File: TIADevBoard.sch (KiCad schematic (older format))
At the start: 41 parts, among them J1 Screw_Terminal_01x02, J2 Conn_Coaxial, J3 Conn_Coaxial, J4 Conn_02x03_Counter_Clockwise, J5 Conn_Coaxial, U1 MC33063AD, U2 OPA2387, U3 ADP3330-3, U4 ADP7183

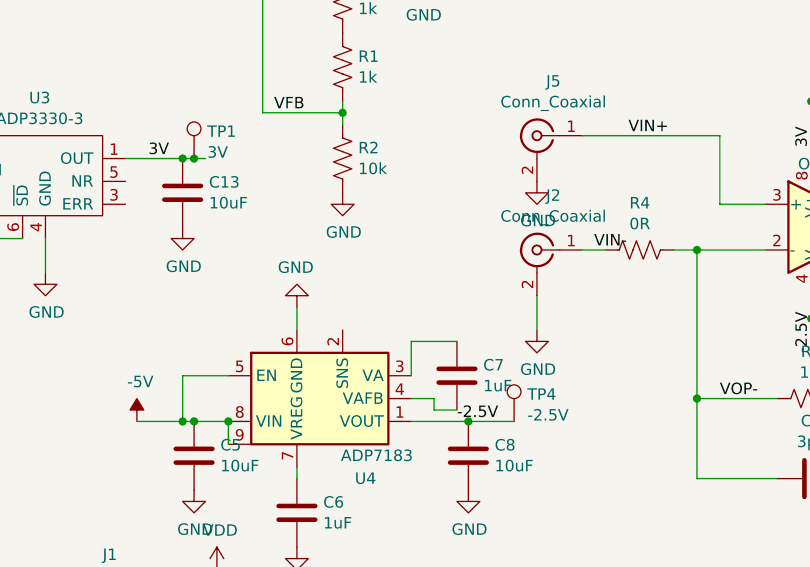
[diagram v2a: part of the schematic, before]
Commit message: fixed some errors in version 3 of PCB, updated the README to that effect.
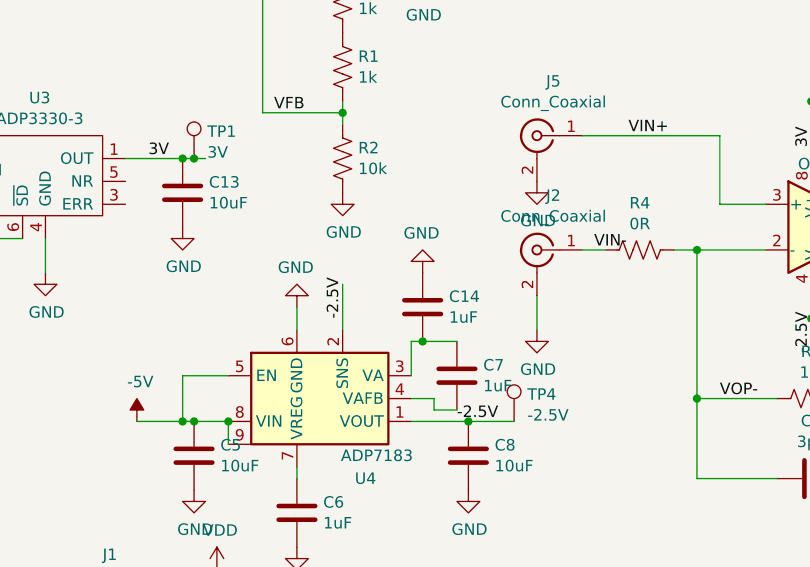
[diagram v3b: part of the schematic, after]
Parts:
- added C14: 1uF, Capacitor_SMD:C_0805_2012Metric_Pad1.15x1.40mm_HandSolder, symbol Device:C
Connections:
- wire segments 102 -> 104
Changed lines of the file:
@@
-$EndComp
-$Comp
-L Device:R_US R2
-U 1 1 6001BAE8
-P 2900 3600
-F 0 "R2" H 2968 3646 50  0000 L CNN
-F 1 "10k" H 2968 3555 50  0000 L CNN
-F 2 "Resistor_SMD:R_0805_2012Metric_Pad1.15x1.40mm_HandSolder" V 2940 3590 50  0001 C CNN
-F 3 "~" H 2900 3600 50  0001 C CNN
-	1    2900 3600
-	1    0    0    -1
 $EndComp
 $Comp
@@
 	3200 4550 3200 4400
 Wire Wire Line
-	3200 4400 3400 4400
+	3200 4400 3250 4400
 Wire Wire Line
 	3200 4650 3300 4650
@@
 Text Label 4150 3500 0    50   ~ 0
 VIN+
+$Comp
+L Device:R_US R2
+U 1 1 6001BAE8
+P 2900 3600
+F 0 "R2" H 2968 3646 50  0000 L CNN
+F 1 "10k" H 2968 3555 50  0000 L CNN
+F 2 "Resistor_SMD:R_0805_2012Metric_Pad1.15x1.40mm_HandSolder" V 2940 3590 50  0001 C CNN
+F 3 "~" H 2900 3600 50  0001 C CNN
+	1    2900 3600
+	1    0    0    -1
+$EndComp
+Wire Wire Line
+	2900 4350 2900 4150
+Text Label 2900 4300 1    50   ~ 0
+-2.5V
+$Comp
+L Device:C C14
+U 1 1 602255CD
+P 3250 4250
+F 0 "C14" H 3365 4296 50  0000 L CNN
+F 1 "1uF" H 3365 4205 50  0000 L CNN
+F 2 "Capacitor_SMD:C_0805_2012Metric_Pad1.15x1.40mm_HandSolder" H 3288 4100 50  0001 C CNN
+F 3 "~" H 3250 4250 50  0001 C CNN
+	1    3250 4250
+	1    0    0    -1
+$EndComp
+Connection ~ 3250 4400
+Wire Wire Line
+	3250 4400 3400 4400
+$Comp
+L power:GND #PWR014
+U 1 1 602262B8
+P 3250 4100
+F 0 "#PWR014" H 3250 3850 50  0001 C CNN
+F 1 "GND" H 3255 3927 50  0000 C CNN
+F 2 "" H 3250 4100 50  0001 C CNN
+F 3 "" H 3250 4100 50  0001 C CNN
+	1    3250 4100
+	-1   0    0    1
+$EndComp
 $EndSCHEMATC

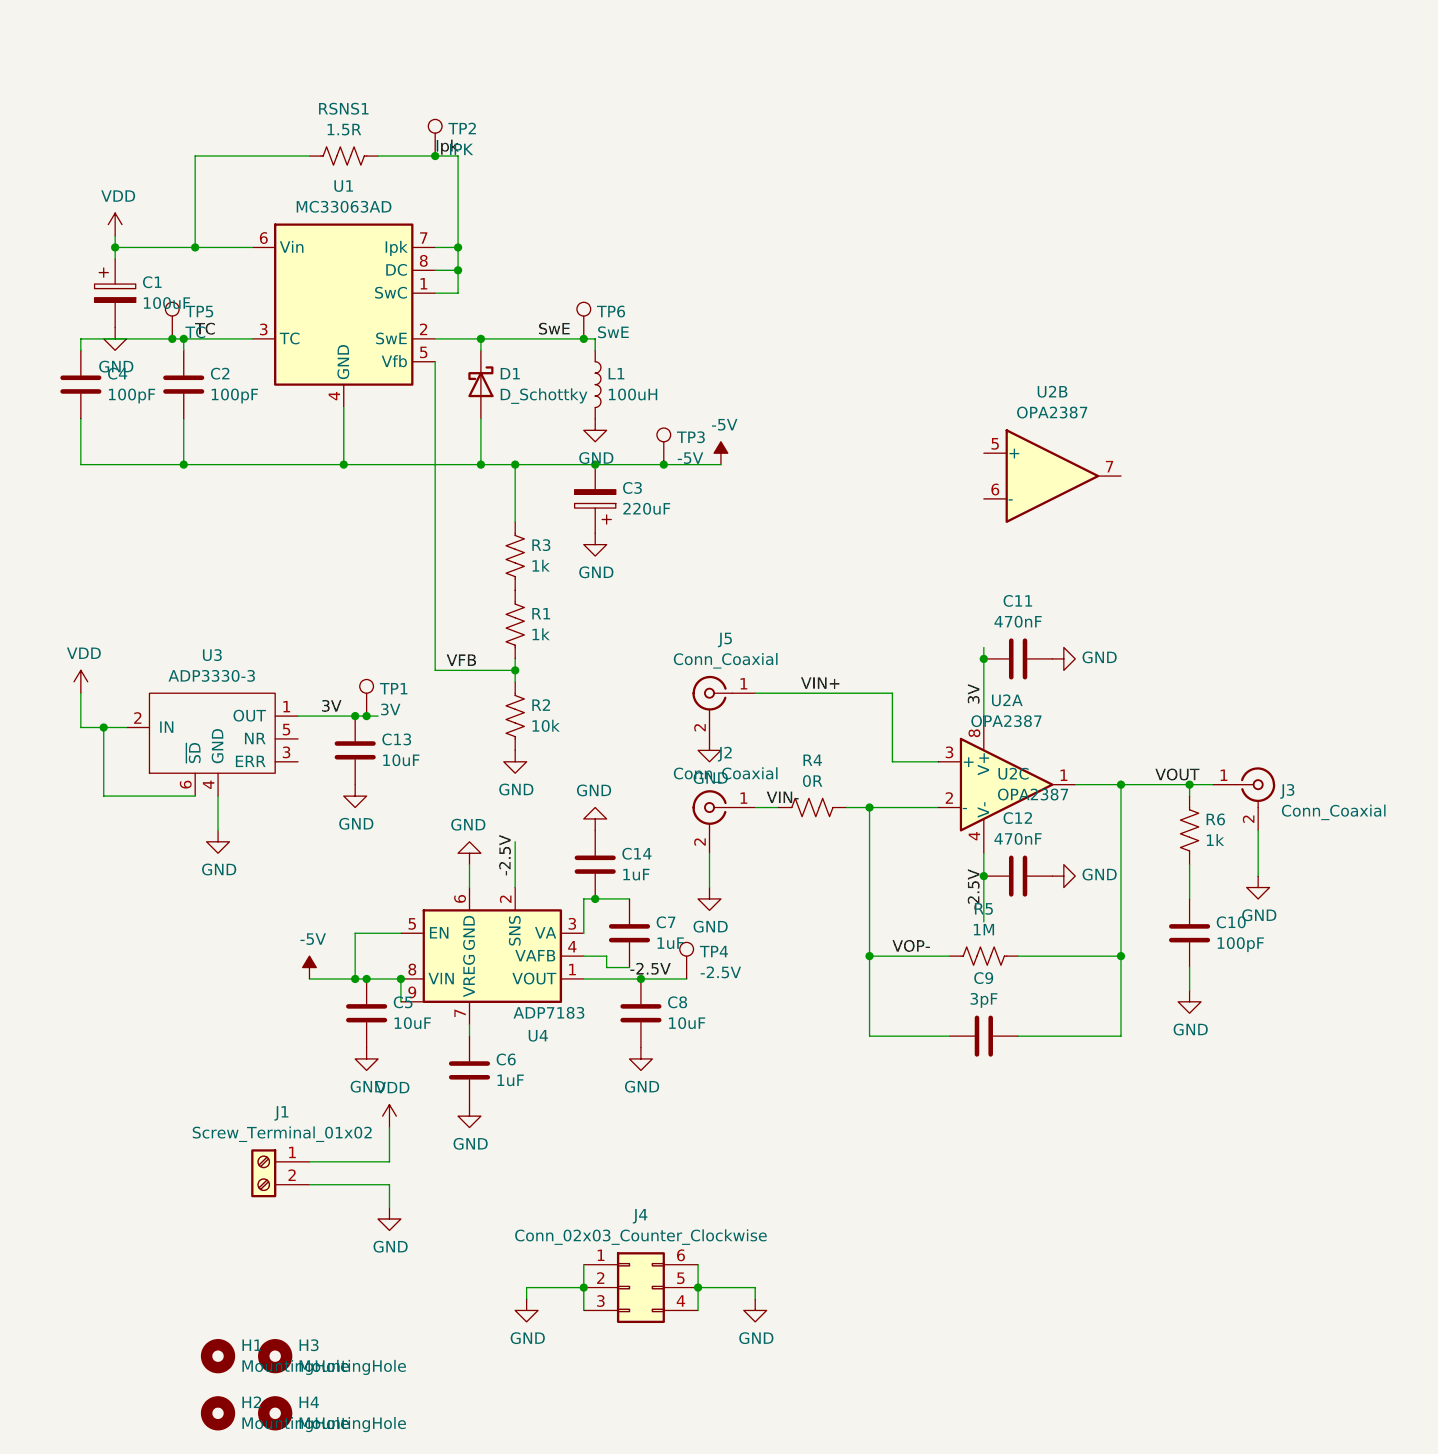
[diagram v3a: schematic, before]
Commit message: partial redesign of TIA v4, removed boost/buck converter, -2.5V linear regulator, added in second opamp in unity gain configuration with bias voltage. Layout not complete.
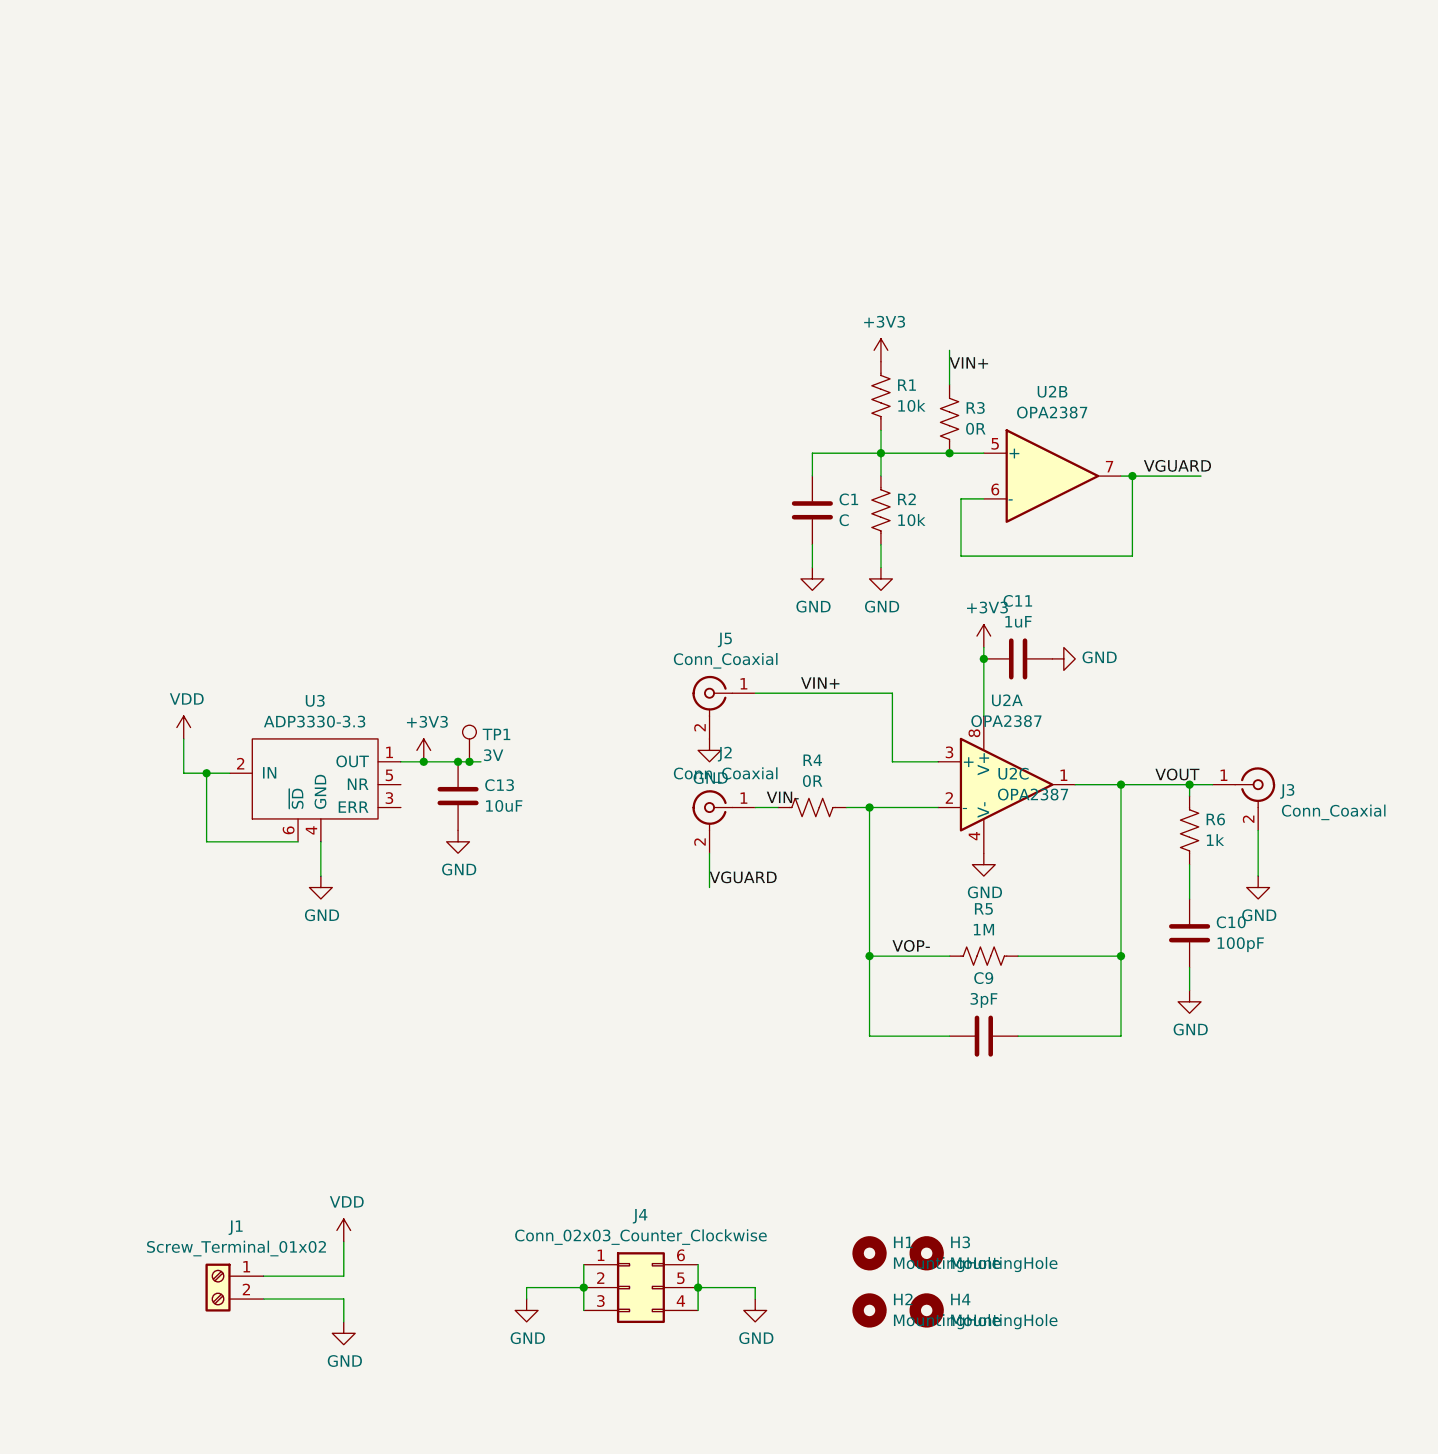
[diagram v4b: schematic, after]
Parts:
- removed C1: 100uF, Capacitor_THT:CP_Radial_D8.0mm_P5.00mm, symbol Device:CP
- removed C12: 470nF, Capacitor_SMD:C_0805_2012Metric_Pad1.15x1.40mm_HandSolder, symbol Device:C
- removed C14, C6, C7: 1uF, Capacitor_SMD:C_0805_2012Metric_Pad1.15x1.40mm_HandSolder, symbol Device:C
- removed C2, C4: 100pF, Capacitor_SMD:C_0805_2012Metric_Pad1.15x1.40mm_HandSolder, symbol Device:C
- removed C3: 220uF, Capacitor_THT:CP_Radial_D8.0mm_P5.00mm, symbol Device:CP
- removed C5, C8: 10uF, Capacitor_SMD:C_0805_2012Metric_Pad1.15x1.40mm_HandSolder, symbol Device:C
- removed D1: D_Schottky, Diode_SMD:D_SMA_Handsoldering, symbol Device:D_Schottky
- removed L1: 100uH, Inductor_SMD:L_1210_3225Metric_Pad1.42x2.65mm_HandSolder, symbol Device:L
- removed RSNS1: 1.5R, Resistor_SMD:R_0805_2012Metric_Pad1.15x1.40mm_HandSolder, symbol Device:R_US
- removed TP2: IPK, my_library_foot:TestPoint_Keystone_5000-5004_Miniature, symbol Connector:TestPoint
- removed TP3: -5V, my_library_foot:TestPoint_Keystone_5000-5004_Miniature, symbol Connector:TestPoint
- removed TP4: -2.5V, my_library_foot:TestPoint_Keystone_5000-5004_Miniature, symbol Connector:TestPoint
- removed TP5: TC, my_library_foot:TestPoint_Keystone_5000-5004_Miniature, symbol Connector:TestPoint
- removed TP6: SwE, my_library_foot:TestPoint_Keystone_5000-5004_Miniature, symbol Connector:TestPoint
- removed U1: MC33063AD, Package_SO:SOIC-8_3.9x4.9mm_P1.27mm, symbol Regulator_Switching:MC33063AD
- removed U4: ADP7183, Package_CSP:LFCSP-8-1EP_2x2mm_P0.5mm_EP1.5x1.0mm, symbol my_library:ADP7183
- added C1: C, Capacitor_SMD:C_0805_2012Metric_Pad1.15x1.40mm_HandSolder, symbol Device:C
- C11: value 470nF -> 1uF
- R1: value 1k -> 10k
- R3: value 1k -> 0R
- U3: value ADP3330-3 -> ADP3330-3.3
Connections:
- net labels added: +3V3, VGUARD
- net labels removed: -2.5V, -5V, 3V, Ipk, SwE, TC, VFB
- wire segments 104 -> 61
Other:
- moved on the sheet: C13, H1, H2, H3, H4, J1, TP1, U3

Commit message: added gerbers for version 5
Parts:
- removed C10: 100pF, Capacitor_SMD:C_0805_2012Metric_Pad1.15x1.40mm_HandSolder, symbol Device:C
- removed J1: Screw_Terminal_01x02, TerminalBlock:TerminalBlock_Altech_AK300-2_P5.00mm, symbol Connector:Screw_Terminal_01x02
- removed J5: Conn_Coaxial, my_library_foot:CON-SMA-EDGE-S, symbol Connector:Conn_Coaxial
- removed R3: 0R, Resistor_SMD:R_0805_2012Metric_Pad1.15x1.40mm_HandSolder, symbol Device:R_US
- removed R6: 1k, Resistor_SMD:R_0805_2012Metric_Pad1.15x1.40mm_HandSolder, symbol Device:R_US
- removed U2: OPA2387, Package_SO:VSSOP-8_3.0x3.0mm_P0.65mm, symbol my_library:OPA2387
- added C3: 1uF, Capacitor_SMD:C_0805_2012Metric_Pad1.15x1.40mm_HandSolder, symbol Device:C
- added C4: 10nF, Capacitor_SMD:C_0805_2012Metric_Pad1.15x1.40mm_HandSolder, symbol Device:C
- added C5, C6, C7: 10uF, Capacitor_SMD:C_0805_2012Metric_Pad1.15x1.40mm_HandSolder, symbol Device:C
- added C8: 100nF, Capacitor_SMD:C_0805_2012Metric_Pad1.15x1.40mm_HandSolder, symbol Device:C
- added CFF1: 100pF, Capacitor_SMD:C_0805_2012Metric_Pad1.15x1.40mm_HandSolder, symbol Device:C
- added D1: D, Diode_SMD:D_SOD-323_HandSoldering, symbol Device:D
- added J1: Jack-DC, Connector_BarrelJack:BarrelJack_Horizontal, symbol Connector:Jack-DC
- added L1, L2, L3: 22uH, Inductor_SMD:L_0805_2012Metric_Pad1.15x1.40mm_HandSolder, symbol Device:L
- added RFB1: 30k, Resistor_SMD:R_0805_2012Metric_Pad1.15x1.40mm_HandSolder, symbol Device:R_US
- added RFB2: 4.7k, Resistor_SMD:R_0805_2012Metric_Pad1.15x1.40mm_HandSolder, symbol Device:R_US
- added TP2: -9V, my_library_foot:TestPoint_Keystone_5000-5004_Miniature, symbol Connector:TestPoint
- added TP3: -5V, my_library_foot:TestPoint_Keystone_5000-5004_Miniature, symbol Connector:TestPoint
- added TP4: -9V_UF, my_library_foot:TestPoint_Keystone_5000-5004_Miniature, symbol Connector:TestPoint
- added TP5: SW, my_library_foot:TestPoint_Keystone_5000-5004_Miniature, symbol Connector:TestPoint
- added TP6: NFB, my_library_foot:TestPoint_Keystone_5000-5004_Miniature, symbol Connector:TestPoint
- added U1: TPS723, Package_TO_SOT_SMD:SOT-23-5_HandSoldering, symbol my_library:TPS723
- added U2: LM2611, Package_TO_SOT_SMD:SOT-23-5_HandSoldering, symbol my_library:LM2611
- added U4: ADA4622, Package_TO_SOT_SMD:SOT-23-5_HandSoldering, symbol my_library:ADA4622
- C1: value C -> 10uF
- C11: value 1uF -> 100nF
- R1: value 10k -> 32k
- R2: value 10k -> 100k
- TP1: value 3V -> 5V
- U3: value ADP3330-3.3 -> ADP3330-5
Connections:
- net labels added: +5V, -5V, -9V, -9V_UF, DTOP, VFB
- net labels removed: +3V3, VGUARD, VIN+
- wire segments 61 -> 101
- no-connect marks 0 -> 2

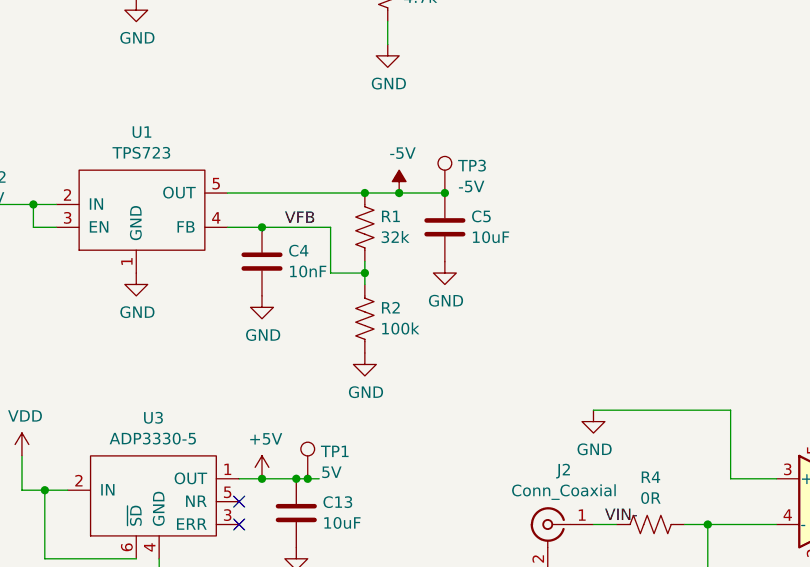
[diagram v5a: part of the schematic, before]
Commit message: updated dev board schematic with correct resistor values
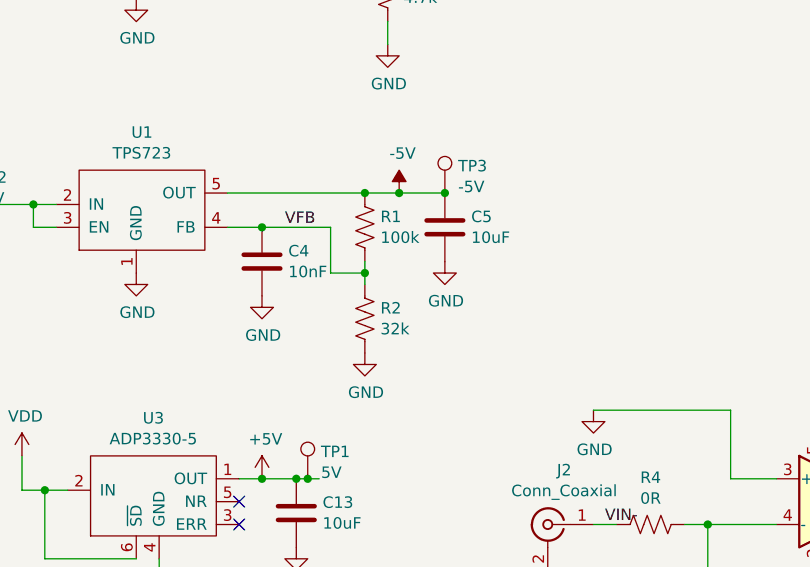
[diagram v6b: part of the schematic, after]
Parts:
- R1: value 32k -> 100k
- R2: value 100k -> 32k
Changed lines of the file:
@@
 P 2950 2700
 F 0 "R1" H 3018 2746 50  0000 L CNN
-F 1 "32k" H 3018 2655 50  0000 L CNN
+F 1 "100k" H 3018 2655 50  0000 L CNN
 F 2 "Resistor_SMD:R_0805_2012Metric_Pad1.15x1.40mm_HandSolder" V 2990 2690 50  0001 C CNN
 F 3 "~" H 2950 2700 50  0001 C CNN
@@
 P 2950 3100
 F 0 "R2" H 3018 3146 50  0000 L CNN
-F 1 "100k" H 3018 3055 50  0000 L CNN
+F 1 "32k" H 3018 3055 50  0000 L CNN
 F 2 "Resistor_SMD:R_0805_2012Metric_Pad1.15x1.40mm_HandSolder" V 2990 3090 50  0001 C CNN
 F 3 "~" H 2950 3100 50  0001 C CNN
